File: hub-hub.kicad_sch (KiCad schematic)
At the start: 37 parts, among them Q4 2N7002, U10 TPS62162DSGR, U11 USB2514B-I/M2, U33 TPS3808G33DBVR, U34 24LC02B-I/SN, Y2 24MHz

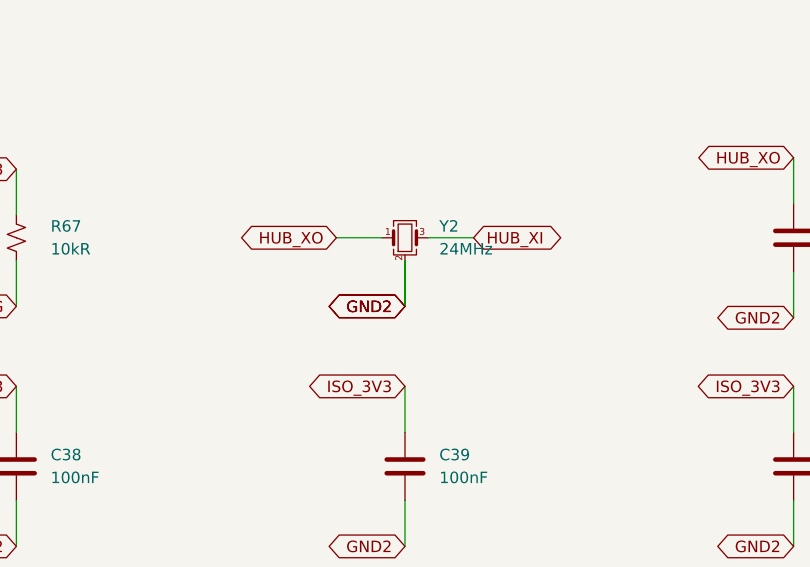
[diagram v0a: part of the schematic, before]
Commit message: feat(revc): assign exact BOM and verified local land patterns
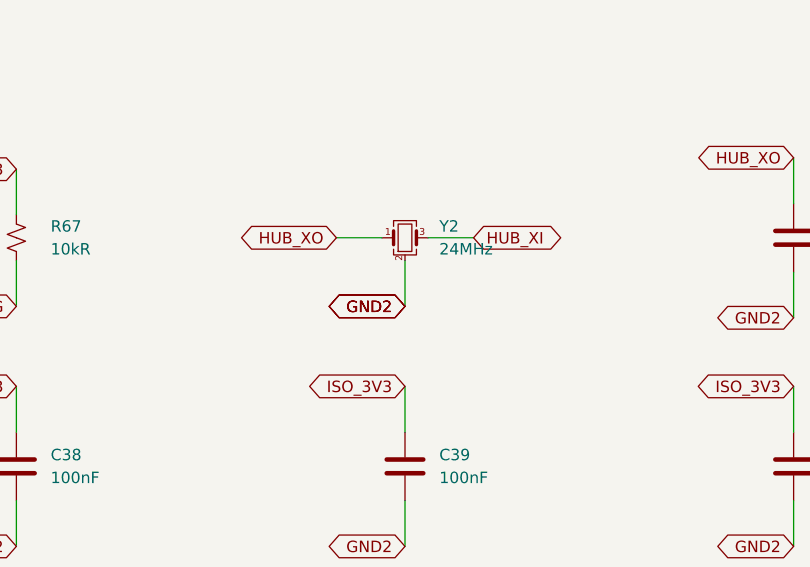
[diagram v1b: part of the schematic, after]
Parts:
- C30: footprint (none) -> hub-lib:C_0805_2012Metric; LCSC (none) -> C84416; MPN (none) -> GRM21BR61E106KA73L; Manufacturer (none) -> Murata Manufacturing; Ratings (none) -> 25V X5R 10%
- C31: footprint (none) -> hub-lib:C_1210_3225Metric; LCSC (none) -> C21397; MPN (none) -> GRM32ER71E226KE15L; Manufacturer (none) -> Murata Manufacturing; Ratings (none) -> 25V X7R 10%
- C32, C33: footprint (none) -> hub-lib:C_0402_1005Metric; LCSC (none) -> C126504; MPN (none) -> GCM1555C1H270JA16D; Manufacturer (none) -> Murata Manufacturing; Ratings (none) -> 50V C0G 5%
- C34, C35, C36, C37, C38, C39, C40, C42, C59, C98: footprint (none) -> hub-lib:C_0402_1005Metric; LCSC (none) -> C77020; MPN (none) -> GRM155R71H104KE14D; Manufacturer (none) -> Murata Manufacturing; Ratings (none) -> 50V X7R 10%
- C41: footprint (none) -> hub-lib:C_0603_1608Metric; LCSC (none) -> C90057; MPN (none) -> GRM188R61E475KE11D; Manufacturer (none) -> Murata Manufacturing; Ratings (none) -> 25V X5R 10%
- D7: footprint LED_SMD:LED_0603_1608Metric -> hub-lib:LED_0603_1608Metric; LCSC (none) -> C125094; Ratings (none) -> See exact manufacturer datasheet
- L2: footprint (none) -> hub-lib:Coilcraft_XFL4020_4x4mm; LCSC (none) -> C122469; Ratings (none) -> See exact manufacturer datasheet
- Q4: footprint Package_TO_SOT_SMD:SOT-23 -> hub-lib:SOT-23; LCSC (none) -> C65189; Ratings (none) -> See exact manufacturer datasheet
- R30: footprint (none) -> hub-lib:R_0402_1005Metric; LCSC (none) -> C409909; MPN (none) -> ERJ2RKF3301X; Manufacturer (none) -> Panasonic Industry; Ratings (none) -> 1%, 0.1W, 50V
- R31: footprint (none) -> hub-lib:R_0402_1005Metric; LCSC (none) -> C192169; MPN (none) -> ERJ2RKF1003X; Manufacturer (none) -> Panasonic Industry; Ratings (none) -> 1%, 0.1W, 50V
- R32: footprint (none) -> hub-lib:R_0402_1005Metric; LCSC (none) -> C413095; MPN (none) -> ERJ2RKF1202X; Manufacturer (none) -> Panasonic Industry; Ratings (none) -> 1%, 0.1W, 50V
- R33, R35, R67: footprint (none) -> hub-lib:R_0402_1005Metric; LCSC (none) -> C191123; MPN (none) -> ERJ2RKF1002X; Manufacturer (none) -> Panasonic Industry; Ratings (none) -> 1%, 0.1W, 50V
- R34, R36: footprint (none) -> hub-lib:R_0402_1005Metric; LCSC (none) -> C400631; MPN (none) -> ERJ2RKF4701X; Manufacturer (none) -> Panasonic Industry; Ratings (none) -> 1%, 0.1W, 50V
- R37: footprint (none) -> hub-lib:R_0402_1005Metric; LCSC (none) -> C242161; MPN (none) -> ERJ2RKF1001X; Manufacturer (none) -> Panasonic Industry; Ratings (none) -> 1%, 0.1W, 50V
- TP12, TP13, TP14, TP15, TP16: footprint TestPoint:TestPoint_Pad_D1.0mm -> hub-lib:TestPoint_Pad_D1.0mm; Manufacturer (none) -> PCB feature; Ratings (none) -> Exposed test pad; no purchased part; now left out of the parts list
- U10: footprint (none) -> hub-lib:Texas_DSG0008A_WSON-8-1EP_2x2mm_P0.5mm_EP0.9x1.6mm; LCSC (none) -> C40256; Ratings (none) -> See exact manufacturer datasheet
- U11: footprint (none) -> hub-lib:Microchip_SQFN36_6x6mm_EP3.7mm; LCSC (none) -> C220679; Ratings (none) -> See exact manufacturer datasheet
- U33: footprint (none) -> hub-lib:SOT-23-6; LCSC (none) -> C43698; Ratings (none) -> See exact manufacturer datasheet
- U34: footprint Package_SO:SOIC-8_3.9x4.9mm_P1.27mm -> hub-lib:SOIC-8_3.9x4.9mm_P1.27mm; LCSC (none) -> C1348870; Ratings (none) -> See exact manufacturer datasheet
- Y2: footprint (none) -> hub-lib:Crystal_SMD_3225-4Pin_3.2x2.5mm; LCSC (none) -> C596911; Ratings (none) -> See exact manufacturer datasheet

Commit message: feat(revc): place synchronized unrouted board and correct bus startup
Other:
- note added: "Declared power origins"
- note added: "EEPROM configuration and programming pads"
- note added: "Host-present reset and VBUS sensing"
- note added: "Hub clock, bias and internal-regulator filters"
- note added: "Hub local bypass: each 100 nF owns one supply pin"
- note added: "Shared 1 A rated 3.3 V buck"
- note added: "USB 2.0 / 480 Mbps | Rev C electrical design | Placement and routing review pending"
- note added: "USB2514B core and per-port control"
- note removed: "Rev C | all routing reserved for Alex | electrical draft under review"
- moved on the sheet: C30, C31, C32, C33, C34, C35, C36, C37, C38, C39, C40, C41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

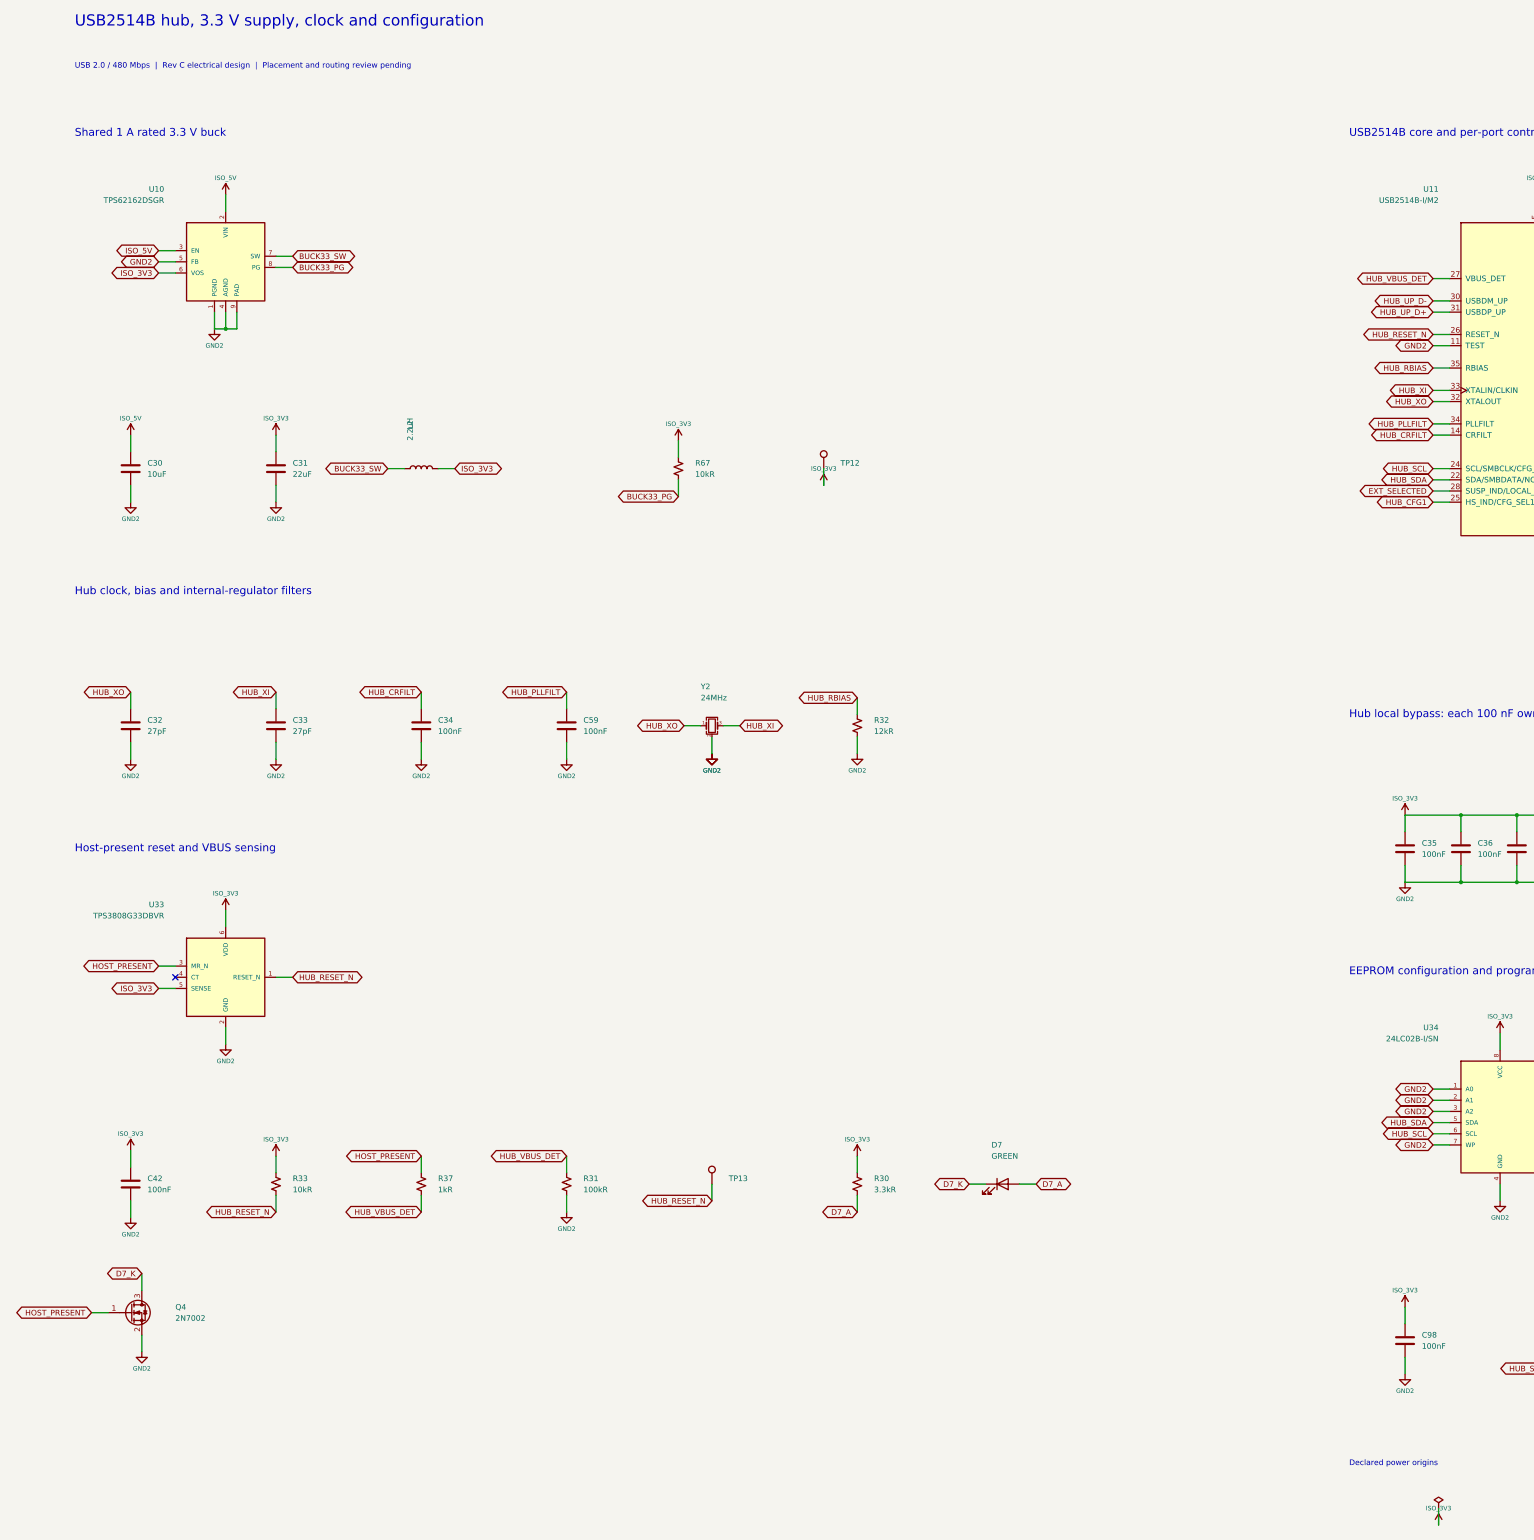
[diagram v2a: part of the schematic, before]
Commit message: feat(revc): finish verified TI hub routing handoff
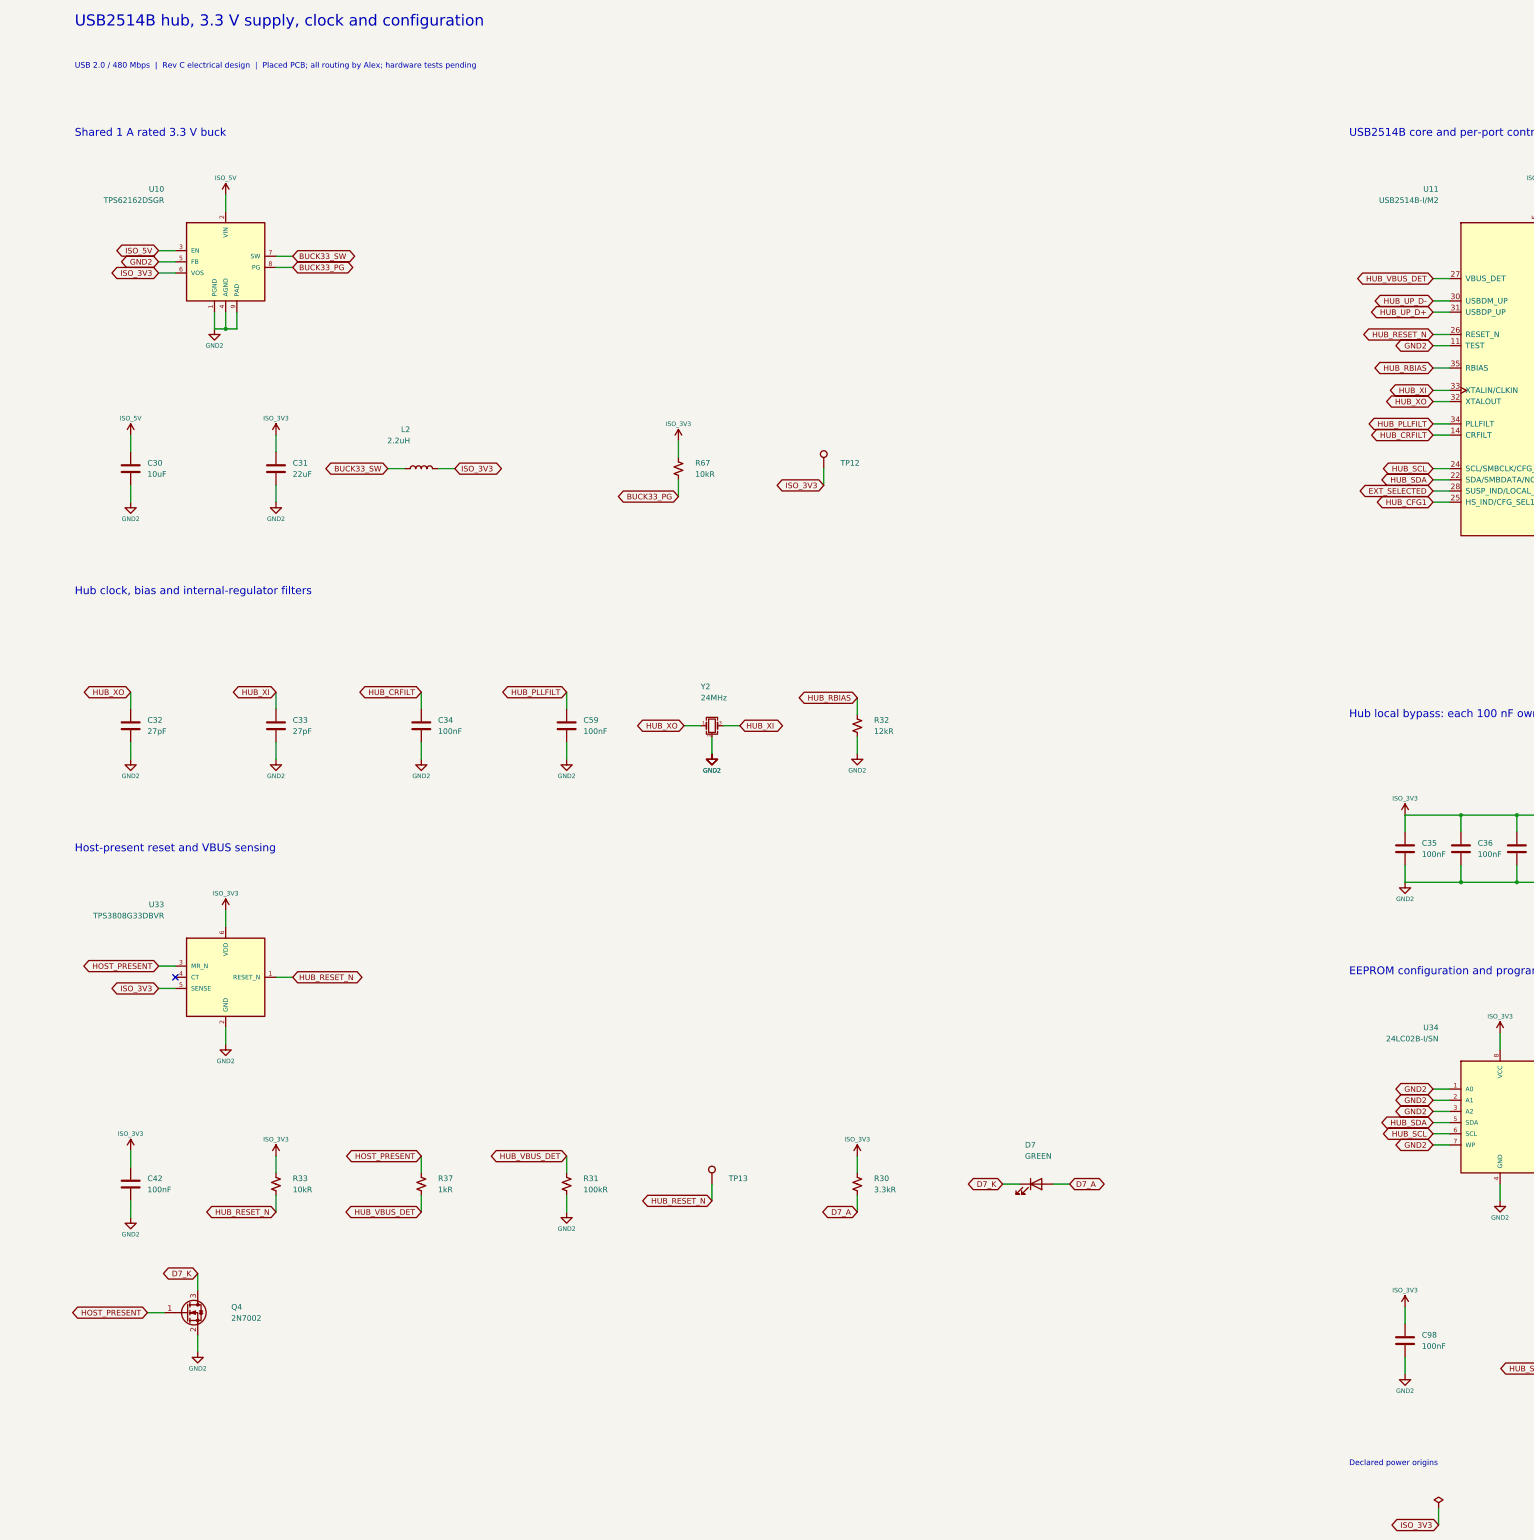
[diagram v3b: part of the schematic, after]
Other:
- note added: "USB 2.0 / 480 Mbps | Rev C electrical design | Placed PCB; all routing by Alex; hardware tests pending"
- note removed: "USB 2.0 / 480 Mbps | Rev C electrical design | Placement and routing review pending"
- moved on the sheet: D7, Q4
